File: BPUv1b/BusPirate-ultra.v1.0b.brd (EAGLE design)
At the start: 100 x 50 mm, 171 parts, among them IC1 23LC1024, IC10 SN74LVC1T45DBV, IC11 SN74LVC1T45DBV, IC12 74LVC1G07DBV, IC13 SN74LVC1T45DBV, IC17 74LVC1G07DBV, IC18 SN74LVC1T45DBV, IC19 74LVC1G07DBV, IC2 23LC1024, IC20 SN74LVC1T45DBV, IC21 74LVC1G07DBV, IC22 SN74LVC1T45DBV, IC23 MCP1824_ADJ, IC24 74HCT4051, IC4 74LVC1G07DBV, IC5 74LVC1G07DBV, IC6 74LVC1G07DBV, IC7 74LVC1G07DBV, IC8 SN74LVC1T45DBV, IC9 SN74LVC1T45DBV, J1 CON_MOLEX_MALE_SMT_SH_1.25, J2 CON_HEADER_1X04, J4 CON_HEADER_1X10-RIGHT_ANGLED_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, Q1 DMMT3906W, U1 W25X40CL, U2 STM32F103ZX, U3 ICE40HX4K, U4 MCP6001, U5 74LVC245A, U7 MCP6001, U8 74HCT4066PW, U9 74HCT4066PW

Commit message: continue routing
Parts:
- removed R10, R7, R8, R9: 10K, resistor:R0603
- added RN1: 10K, dp_devices:RN8P-4R-CRA06S
- moved R44 4.83 mm to (34.7, 3.94)
- moved R41 4.70 mm to (69.1, 7.75), turned to 0 degrees
- moved Q1 4.04 mm to (37.5, 3.81), turned to 90 degrees
- moved R43 4.03 mm to (40.3, 3.81), turned to 90 degrees
- moved C60 3.94 mm to (72.1, 7.75), turned to 0 degrees
- moved Q2 3.90 mm to (37.3, 7.49)
- moved C59 3.86 mm to (67.1, 6.60), turned to 270 degrees
- moved R38 3.49 mm to (79.0, 8.89), turned to 0 degrees
- moved C9 2.79 mm to (29.8, 11.7)
- moved C58 2.47 mm to (82.3, 7.75), turned to 0 degrees
- moved C55 2.42 mm to (68.3, 16.5)
- moved R35 2.42 mm to (71.4, 16.5), turned to 0 degrees
- moved C3 2.29 mm to (33.8, 11.6)
- moved C56 2.07 mm to (74.4, 16.5), turned to 0 degrees
- moved IC21 2.03 mm to (70.4, 3.05)
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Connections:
- removed net N$65: R51.2, R9.1
- new net N$21: R51.2, RN1.4
- net ADC1: now also RN1.5, RN1.6; no longer R10.2, R9.2
- net GND: now also RN1.2, RN1.3; no longer R10.1, R8.1
- net MCU_ADC6: now also RN1.7, RN1.8; no longer R7.2, R8.2
- net VREF/VOUT: now also RN1.1; no longer R7.1
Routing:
- net VUSB: track 120.9 -> 258.8 mm, vias 7 -> 14
- net VREF/VOUT: track 56.3 -> 117.6 mm, vias 0 -> 2
- net N$26: track 0.00 -> 23.7 mm, vias 0 -> 4
- net ADC1: track 32.3 -> 10.6 mm, vias 2 -> 0
- net MCU_ADC6: track 0.00 -> 21.3 mm, vias 0 -> 2
- net MCU_VPU: track 0.00 -> 15.2 mm, vias 0 -> 4
- net N$11: track 0.00 -> 6.62 mm
- net N$21: track 0.00 -> 6.62 mm
- net N$12: track 0.00 -> 5.77 mm
- net N$25: track 0.00 -> 3.90 mm
- net N$27: track 0.00 -> 3.49 mm
- net BUFOD7: track 25.1 -> 21.7 mm
- net 3V3: track 409.2 -> 406.7 mm, vias 33 -> 35
- net BUFDIR7: track 24.5 -> 22.4 mm
- net BUFIO7: track 20.8 -> 18.8 mm
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- added copper zone on layer 1, net N$26
- added copper zone on layer 1, net VREF/VOUT

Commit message: routed power traces
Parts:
- moved C48 2.34 mm to (82.5, 16.5), turned to 180 degrees
- moved C54 1.35 mm to (71.1, 26.9)
- moved R32 1.30 mm to (82.5, 17.7)
- moved R42 1.14 mm to (75.1, 3.81), turned to 90 degrees
- moved R39 0.89 mm to (85.2, 3.30)
- moved C42 0.65 mm to (79.2, 16.5), turned to 0 degrees
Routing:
- net 3V3: track 406.7 -> 562.3 mm, vias 35 -> 64
- net VREF/VOUT: track 117.6 -> 186.4 mm, vias 2 -> 14
- net MCU_VPU: track 15.2 -> 53.0 mm, vias 4 -> 6
- net BPIO7: track 52.5 -> 59.0 mm
- net BPIO1: track 62.1 -> 59.1 mm, vias 3 -> 4
- net BPIO4: track 54.7 -> 57.7 mm
- net N$5: track 8.93 -> 11.2 mm
- net BPIO6: track 56.0 -> 58.2 mm, vias 4 -> 5
- net VUSB: track 258.8 -> 256.9 mm
- net BUFDIR4: track 21.1 -> 22.3 mm
- net BUFDIR7: track 22.4 -> 21.3 mm
- net BUFIO4: track 17.5 -> 18.3 mm
- net BUFDIR1: track 19.1 -> 19.7 mm
- net BUFOD4: track 19.3 -> 19.8 mm

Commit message: continue routing
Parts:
- R6: device dp_devices:R603 -> rcl:R0603
- moved R16 11.5 mm to (51.3, 7.87), turned to 180 degrees
- moved R15 9.45 mm to (50.8, 10.4)
- moved R51 4.45 mm to (44.2, 3.43)
- moved C22 2.95 mm to (63.0, 11.2), flipped to the bottom
- moved C14 2.85 mm to (47.6, 4.95), turned to 270 degrees
- moved R6 2.01 mm to (65.9, 12.1), turned to 90 degrees
- moved C30 1.37 mm to (48.8, 10.4)
- moved C51 1.14 mm to (49.7, 4.95), turned to 270 degrees
- moved C33 0.80 mm to (46.7, 10.4)
- moved RN1 0.76 mm to (44.2, 6.60)
- moved Q2 0.51 mm to (37.3, 6.99)
- moved Q1 0.25 mm to (37.5, 3.56)
- moved R43 0.25 mm to (40.3, 3.56)
- moved R44 0.25 mm to (34.7, 3.68)
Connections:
- net FPGA_PROG_CS: now also R6.2; no longer R6.1
- net GND: now also R6.1; no longer R6.2
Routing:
- net MCU_VPU: track 53.0 -> 119.5 mm, vias 6 -> 9
- net N$61: track 0.00 -> 42.5 mm, vias 0 -> 4
- net ADC1: track 10.6 -> 31.4 mm, vias 0 -> 2
- net MCU_ADC6: track 21.3 -> 34.8 mm
- net 3V3: track 562.3 -> 557.5 mm
- net N$21: track 6.62 -> 2.01 mm
- net N$64: track 5.97 -> 10.5 mm
- net FPGA_PROG_CS: track 36.4 -> 38.9 mm
- net BPIO6: track 58.2 -> 60.7 mm, vias 5 -> 3
- net FPGA_CRESET: track 33.0 -> 35.3 mm, vias 2 -> 3
- net N$26: track 23.7 -> 25.5 mm
- net BUFIO7: track 18.8 -> 17.2 mm
- net BUFDIR7: track 21.3 -> 19.9 mm
- net BUFIO6: track 28.4 -> 27.0 mm
- net BUFOD6: track 31.5 -> 30.2 mm
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
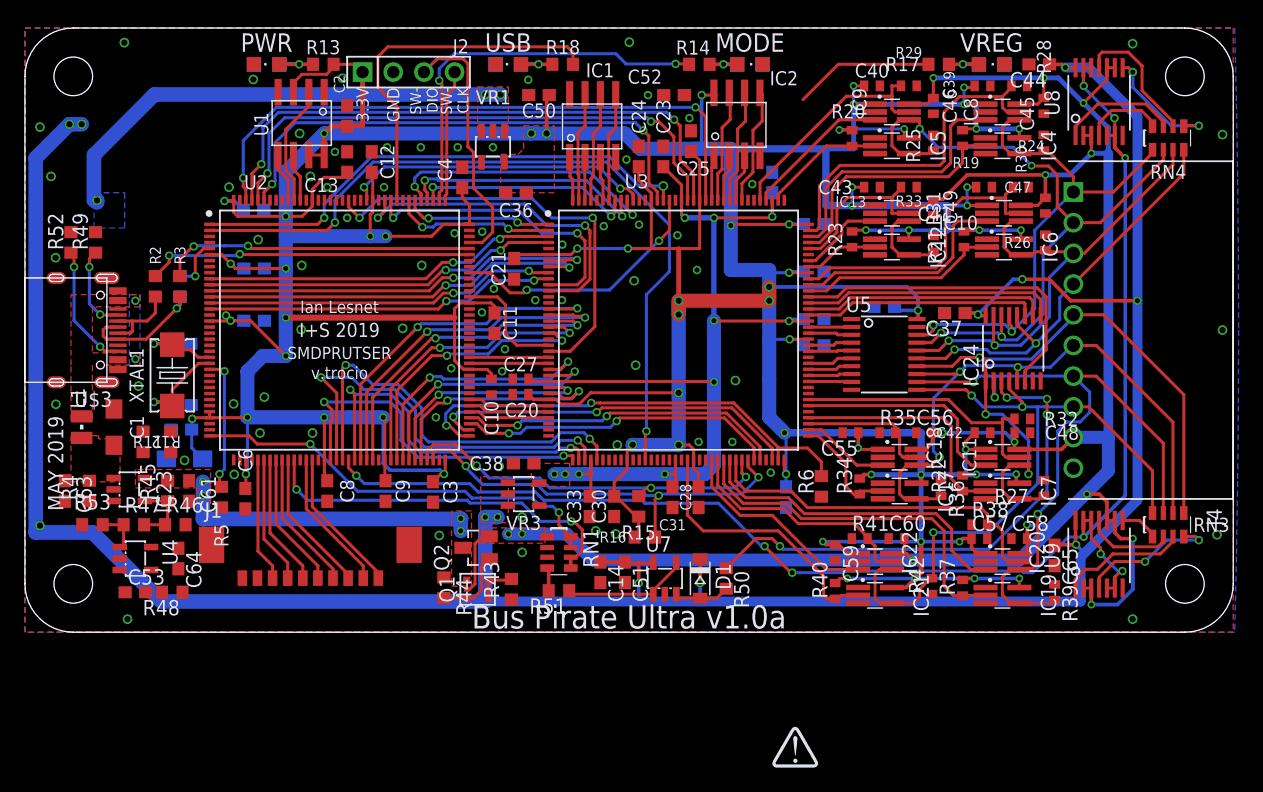
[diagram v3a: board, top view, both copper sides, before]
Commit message: board routing done, add usbc bottom PTH chassis mount library
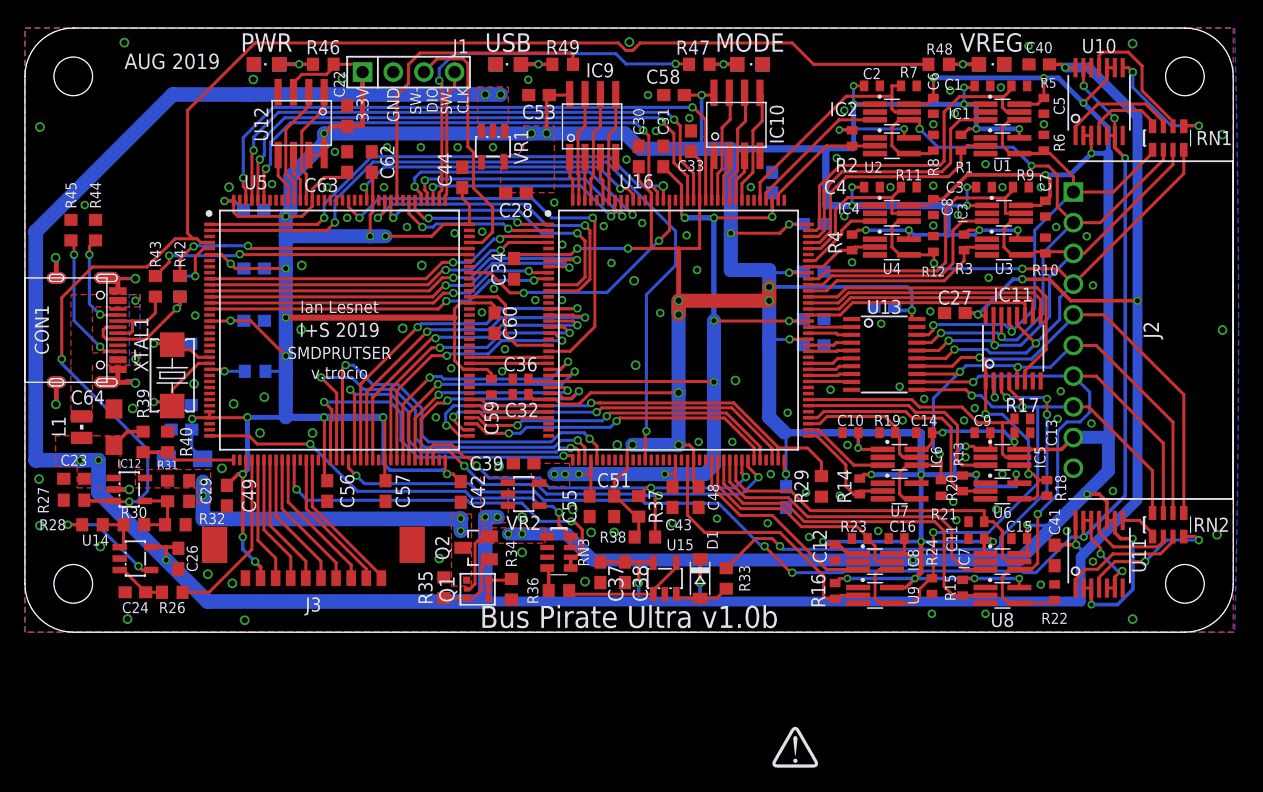
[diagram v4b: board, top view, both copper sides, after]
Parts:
- removed C65: 0.1uF, rcl:C0603
- removed IC13, IC18, IC20, IC22: SN74LVC1T45DBV, dp_devices.v6:SC-70-6_EXTENDED_PADS
- removed IC17, IC19, IC21: 74LVC1G07DBV, dp_devices.v6:SC-70-5_EXTENDED_PADS
- removed IC23: MCP1824_ADJ, dp_devices.v6:SOT-23-5
- removed IC24: 74HCT4051, dp_devices.v6:TSSOP-16
- removed J4: CON_HEADER_1X10-RIGHT_ANGLED_PTH_SHROUDED, dp_devices.v6:M1X10_MALE_RIGHT_ANGLES_PTH_SHROUDED
- removed R50, R51: (no value), resistor:R0603
- removed R52: 5K1, rcl:R0603
- removed R53: 0R, dp_devices.v6:R603
- removed RN4: 2K, dp_devices:RN8P-4R-CRA06S
- added C62: 0.1uF, rcl:C0603
- added IC3: SN74LVC1T45DBV, dp_devices.v6:SC-70-6_EXTENDED_PADS
- added J3: CON_MOLEX_MALE_SMT_SH_1.25, dp_devices.v6:MOLEX_533980771
- added R10, R8: 1M, resistor:R0402
- added R7, R9: 100K, resistor:R0402
- added RN2: 2K, dp_devices:RN8P-4R-CRA06S
- added U10, U11: 74HCT4066PW, dp_devices.v6:TSSOP-14
- added U12: W25X40CL, dp_devices.v6:SOIC-8
- added U13: 74LVC245A, dp_devices.v6:TSSOP-20
- added U14, U15: MCP6001, dp_devices.v6:SOT-23-5
- added U16: ICE40HX4K, dp_devices.v6:TQFP-144
- added U6: 74LVC1G07DBV, dp_devices.v6:SC-70-5_EXTENDED_PADS
- C1: value 10uF -> 0.1uF; device rcl:SMC_A -> rcl:C0402
- C10: device dp_devices.v6:C402 -> resistor:C0402
- C11, C12, C13, C14, C15, C2, C3, C4, C6, C7, C8, C9: device rcl:C0603 -> resistor:C0402
- C16: value 22pF -> 0.1uF; device rcl:C0603 -> resistor:C0402
- C17: value 1uF -> 0.1uF; device rcl:SMC_A -> rcl:C0603
- C19: value 0.1uF -> 1uF; device rcl:C0603 -> rcl:SMC_A
- C20: value 0.1uF -> 22pF; device dp_devices.v6:C402 -> rcl:C0603
- C23: value 0.1uF -> 10uF; device rcl:C0603 -> dp_devices.v6:C603
- C24: value 0.1uF -> (none)
- C27: device dp_devices.v6:C402 -> rcl:C0603
- C28: value 0.1uF -> 1uf
- C29: value 0.1uF -> 1uF; device rcl:C0603 -> dp_devices.v6:C603
- C32: device rcl:C0603 -> dp_devices.v6:C402
- C36: value 1uf -> 0.1uF; device rcl:C0603 -> dp_devices.v6:C402
- C38: value 1uf -> 1uF
- C39: value 0.1uF -> 1uf; device rcl:C0402 -> rcl:C0603
- C40, C41, C42, C43, C46, C47, C48, C49, C55, C56, C57, C58, C60: device resistor:C0402 -> rcl:C0603
- C45: device rcl:C0402 -> rcl:C0603
- C5: device rcl:C0603 -> rcl:C0402
- C51: value 1uF -> 0.1uF
- C53: value (none) -> 0.1uF
- C59: device resistor:C0402 -> dp_devices.v6:C402
- C61: value 1uF -> 0.1uF; device dp_devices.v6:C603 -> rcl:C0603
- C63: value 10uF -> 0.1uF; device dp_devices.v6:C603 -> rcl:C0603
- C64: value 0.1uF -> 10uF; device rcl:C0603 -> rcl:SMC_A
- IC1, IC2: value 23LC1024 -> SN74LVC1T45DBV; device dp_devices:SOIC-8 -> dp_devices.v6:SC-70-6_EXTENDED_PADS
- IC10, IC9: value SN74LVC1T45DBV -> 23LC1024; device dp_devices.v6:SC-70-6_EXTENDED_PADS -> dp_devices:SOIC-8
- IC11: value SN74LVC1T45DBV -> 74HCT4051; device dp_devices.v6:SC-70-6_EXTENDED_PADS -> dp_devices.v6:TSSOP-16
- IC12: value 74LVC1G07DBV -> MCP1824_ADJ; device dp_devices.v6:SC-70-5_EXTENDED_PADS -> dp_devices.v6:SOT-23-5
- IC4, IC5, IC6, IC7: value 74LVC1G07DBV -> SN74LVC1T45DBV; device dp_devices.v6:SC-70-5_EXTENDED_PADS -> dp_devices.v6:SC-70-6_EXTENDED_PADS
- J1: value CON_MOLEX_MALE_SMT_SH_1.25 -> CON_HEADER_1X04; device dp_devices.v6:MOLEX_533980771 -> dp_devices.v6:M1X4
- J2: value CON_HEADER_1X04 -> CON_HEADER_1X10-RIGHT_ANGLED_PTH_SHROUDED; device dp_devices.v6:M1X4 -> dp_devices.v6:M1X10_MALE_RIGHT_ANGLES_PTH_SHROUDED
- R1: value 1.5K -> 100K; device rcl:R0603 -> resistor:R0402
- R11: value 10K -> 100K; device resistor:R0603 -> resistor:R0402
- R12: value 10K -> 1M; device resistor:R0603 -> resistor:R0402
- R13, R14, R17: value 1K1 -> 100K; device dp_devices:R603 -> resistor:R0402
- R15, R16: value 10K -> 100K; device rcl:R0603 -> resistor:R0402
- R18: value 1K1 -> 1M; device dp_devices:R603 -> resistor:R0402
- R2, R3: value 22R -> 100K; device rcl:R0603 -> resistor:R0402
- R20, R22: value 100K -> 1M
- R25, R27: value 1M -> 10K; device resistor:R0402 -> dp_devices.v6:R603
- R26: value 1M -> (none); device resistor:R0402 -> rcl:R0603
- R28: value 100K -> 0R; device resistor:R0402 -> dp_devices.v6:R603
- R29, R37, R38: value 100K -> 10K; device resistor:R0402 -> rcl:R0603
- R30: value 100K -> 78.7K; device resistor:R0402 -> dp_devices.v6:R603
- R31: value 1M -> 100K; device resistor:R0402 -> dp_devices.v6:R603
- R32: value 100K -> 50K; device resistor:R0402 -> dp_devices.v6:R603
- R33: value 100K -> (none); device resistor:R0402 -> resistor:R0603
- R34, R35: value 100K -> (none); device resistor:R0402 -> dp_devices.v6:R603
- R36: value 1M -> (none); device resistor:R0402 -> resistor:R0603
- R39: value 1M -> 10K; device resistor:R0402 -> resistor:R0603
- R4, R5: value 10K -> 100K; device dp_devices.v6:R603 -> resistor:R0402
- R40: value 100K -> 10K; device resistor:R0402 -> resistor:R0603
- R41: value 100K -> 1.5K; device resistor:R0402 -> rcl:R0603
- R42: value 1M -> 22R; device resistor:R0402 -> rcl:R0603
- R43: value (none) -> 22R; device dp_devices.v6:R603 -> rcl:R0603
- R44: value (none) -> 5K1; device dp_devices.v6:R603 -> rcl:R0603
- R45: value 100K -> 5K1; device dp_devices.v6:R603 -> rcl:R0603
- R46: value 50K -> 1K1; device dp_devices.v6:R603 -> dp_devices:R603
- R47: value 78.7K -> 1K1; device dp_devices.v6:R603 -> dp_devices:R603
- R48: value (none) -> 1K1; device rcl:R0603 -> dp_devices:R603
- R49: value 5K1 -> 1K1; device rcl:R0603 -> dp_devices:R603
- R6: value 10K -> 1M; device rcl:R0603 -> resistor:R0402
- RN1: value 10K -> 2K
- RN3: value 2K -> 10K
- U1: value W25X40CL -> 74LVC1G07DBV; device dp_devices.v6:SOIC-8 -> dp_devices.v6:SC-70-5_EXTENDED_PADS
- U2: value STM32F103ZX -> 74LVC1G07DBV; device dp_devices.v6:TQFP-144 -> dp_devices.v6:SC-70-5_EXTENDED_PADS
- U3: value ICE40HX4K -> 74LVC1G07DBV; device dp_devices.v6:TQFP-144 -> dp_devices.v6:SC-70-5_EXTENDED_PADS
- U4, U7: value MCP6001 -> 74LVC1G07DBV; device dp_devices.v6:SOT-23-5 -> dp_devices.v6:SC-70-5_EXTENDED_PADS
- U5: value 74LVC245A -> STM32F103ZX; device dp_devices.v6:TSSOP-20 -> dp_devices.v6:TQFP-144
- U8, U9: value 74HCT4066PW -> 74LVC1G07DBV; device dp_devices.v6:TSSOP-14 -> dp_devices.v6:SC-70-5_EXTENDED_PADS
- moved R28 84.9 mm to (5.59, 8.89), turned to 0 degrees
- moved R27 80.3 mm to (4.06, 10.9), turned to 180 degrees
- moved R30 78.5 mm to (9.02, 8.89), turned to 0 degrees
- moved R26 77.8 mm to (12.2, 3.30), turned to 180 degrees
- moved C1 77.2 mm to (79.2, 45.2), turned to 0 degrees
- moved R48 77.0 mm to (75.6, 47.0)
- moved R39 76.5 mm to (9.78, 15.7)
- moved R5 74.3 mm to (82.3, 45.2), turned to 180 degrees
- moved R32 70.6 mm to (12.4, 8.89), turned to 0 degrees
- moved C15 69.9 mm to (82.3, 7.75), flipped to the top, turned to 0 degrees
- moved J2 68.7 mm to (93.2, 25.0), turned to 270 degrees
- moved U4 67.7 mm to (71.8, 31.9)
- moved R12 67.4 mm to (75.2, 32.1)
- moved R42 67.0 mm to (12.8, 28.6), turned to 270 degrees
- moved R31 66.6 mm to (11.8, 11.7), turned to 90 degrees
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- renumbered U$3 to CON1, VR3 to VR2
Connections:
- net 1V2: now also C36.1, C39.1, C43.2, C54.2, C55.2, U16.111, U16.126, U16.27, U16.40, U16.54, U16.92; no longer C23.2, C26.2, C27.1, C33.2, C38.1, U3.111, U3.126, U3.27, U3.40, U3.54, U3.92
- net 3V3: now also C1.1, C11.1, C12.1, C17.2, C19.+, C2.1, C28.1, C3.1, C32.1, C33.2, C4.1, C42.2, C44.2, C45.2, C46.2, C47.2, C48.2, C49.2, C50.2, C51.2, C52.2, C53.1, C56.2, C57.2, C58.1, C60.2, C61.1, C62.2, C63.2, C9.1, IC1.1, IC10.8, IC2.1, IC3.1, IC4.1, IC5.1, IC6.1, IC7.1, IC9.8, J1.1, J3.P9, R1.2, R14.2, R2.2, R25.2, R3.2, R38.2, R4.2, R46.2, U1.5, U12.3, U12.7, U12.8, U13.20, U16.100, U16.108, U16.123, U16.131, U16.30, U16.46, U16.57, U16.6, U16.72, U16.89, U2.5, U3.5, U4.5, U5.108, U5.121, U5.131, U5.144, U5.17, U5.32, U5.33, U5.39, U5.52, U5.6, U5.62, U5.72, U5.84, U5.95, U6.5, U7.5, U8.5, U9.5; no longer C11.2, C12.2, C13.2, C15.2, C17.+, C19.2, C2.2, C20.1, C24.2, C28.2, C29.2, C3.2, C32.2, C36.1, C39.1, C4.2, C40.1, C41.1, C42.1, C43.1, C5.2, C50.1, C52.1, C54.1, C55.1, C57.1, C6.2, C7.2, C8.2, C9.2, IC1.8, IC10.1, IC11.1, IC12.5, IC13.1, IC17.5, IC18.1, IC19.5, IC2.8, IC20.1, IC21.5, IC22.1, IC4.5, IC5.5, IC6.5, IC7.5, IC9.1, J1.P9, J2.1, R19.2, R20.2, R21.2, R22.2, R23.2, R34.2, R40.2, R5.2, U1.3, U1.7, U1.8, U2.108, U2.121, U2.131, U2.144, U2.17, U2.32, U2.33, U2.39, U2.52, U2.6, U2.62, U2.72, U2.84, U2.95, U3.100, U3.108, U3.123, U3.131, U3.30, U3.46, U3.57, U3.6, U3.72, U3.89, U5.20
- net ADC1: now also RN3.5, RN3.6, U5.47; no longer RN1.5, RN1.6, U2.47
- net ADC_MUX_EN: now also IC11.6, U16.96; no longer IC24.6, U3.96
- net ADC_MUX_S0: now also IC11.11, U16.93; no longer IC24.11, U3.93
- net ADC_MUX_S1: now also IC11.10, U16.94; no longer IC24.10, U3.94
- net ADC_MUX_S2: now also IC11.9, U16.95; no longer IC24.9, U3.95
- net BPIO0: now also IC1.4, IC11.13, J2.1, R6.2, RN1.1, U1.4, U13.18; no longer IC24.13, IC4.4, IC8.4, J4.1, R24.2, RN4.1, U5.18
- net BPIO1: now also IC11.14, IC2.4, J2.2, R8.2, RN1.2, U13.17, U2.4; no longer IC24.14, IC5.4, IC9.4, J4.2, R25.2, RN4.2, U5.17
- net BPIO2: now also IC11.15, IC3.4, J2.3, R10.2, RN1.3, U13.16, U3.4; no longer IC10.4, IC24.15, IC6.4, J4.3, R26.2, RN4.3, U5.16
- net BPIO3: now also IC11.12, IC4.4, J2.4, R12.2, RN1.4, U13.15, U4.4; no longer IC12.4, IC13.4, IC24.12, J4.4, R31.2, RN4.4, U5.15
- net BPIO4: now also IC11.1, IC5.4, J2.5, R18.2, RN2.5, U13.14, U6.4; no longer IC11.4, IC24.1, IC7.4, J4.5, R27.2, RN3.5, U5.14
- net BPIO5: now also IC11.5, IC6.4, J2.6, R20.2, RN2.6, U13.13, U7.4; no longer IC17.4, IC18.4, IC24.5, J4.6, R36.2, RN3.6, U5.13
- net BPIO6: now also IC11.2, IC7.4, J2.7, R22.2, RN2.7, U13.12, U8.4; no longer IC19.4, IC20.4, IC24.2, J4.7, R39.2, RN3.7, U5.12
- net BPIO7: now also IC11.4, IC8.4, J2.8, R24.2, RN2.8, U13.11, U9.4; no longer IC21.4, IC22.4, IC24.4, J4.8, R42.2, RN3.8, U5.11
- net BUFDIR0: now also IC1.5, R5.2, U16.107; no longer IC8.5, R28.2, U3.107
- net BUFDIR1: now also IC2.5, R7.2, U16.113; no longer IC9.5, R29.2, U3.113
- net BUFDIR2: now also IC3.5, R9.2, U16.99; no longer IC10.5, R30.2, U3.99
- net BUFDIR3: now also IC4.5, R11.2, U16.104; no longer IC13.5, R33.2, U3.104
- net BUFDIR4: now also IC5.5, R17.2, U16.79; no longer IC11.5, R32.2, U3.79
- net BUFDIR5: now also IC6.5, R19.2, U16.75; no longer IC18.5, R35.2, U3.75
- net BUFDIR6: now also IC7.5, R21.2, U16.64; no longer IC20.5, R38.2, U3.64
- net BUFDIR7: now also IC8.5, R23.2, U16.61; no longer IC22.5, R41.2, U3.61
- net BUFIO0: now also IC1.3, U16.106; no longer IC8.3, U3.106
- net BUFIO1: now also IC2.3, U16.112; no longer IC9.3, U3.112
- net BUFIO2: now also IC3.3, U16.98; no longer IC10.3, U3.98
- net BUFIO3: now also IC4.3, U16.102; no longer IC13.3, U3.102
- net BUFIO4: now also IC5.3, U16.78; no longer IC11.3, U3.78
- net BUFIO5: now also IC6.3, U16.74; no longer IC18.3, U3.74
- net BUFIO6: now also IC7.3, U16.63; no longer IC20.3, U3.63
- net BUFIO7: now also IC8.3, U16.60; no longer IC22.3, U3.60
- net BUFOD0: now also R1.1, U1.2, U16.105; no longer IC4.2, R19.1, U3.105
- net BUFOD1: now also R2.1, U16.110, U2.2; no longer IC5.2, R20.1, U3.110
- net BUFOD2: now also R3.1, U16.97, U3.2; no longer IC6.2, R21.1, U3.97
- net BUFOD3: now also R4.1, U16.101, U4.2; no longer IC12.2, R23.1, U3.101
- net BUFOD4: now also R13.1, U16.76, U6.2; no longer IC7.2, R22.1, U3.76
- net BUFOD5: now also R14.1, U16.73, U7.2; no longer IC17.2, R34.1, U3.73
- net BUFOD6: now also R15.1, U16.62, U8.2; no longer IC19.2, R37.1, U3.62
- net BUFOD7: now also R16.1, U16.56, U9.2; no longer IC21.2, R40.1, U3.56
- net D+: now also R41.1, R42.2; no longer R1.1, R3.2
- net D-: now also R43.2; no longer R2.2
- net DISPLAY_AUX1: now also J3.P5, U5.44; no longer J1.P5, U2.44
- net DISPLAY_AUX2: now also J3.P4, U5.45; no longer J1.P4, U2.45
- net DISPLAY_CS: now also J3.P1, U5.50; no longer J1.P1, U2.50
- net DISPLAY_D/P: now also J3.P2, U5.49; no longer J1.P2, U2.49
- net DISPLAY_PWM: now also J3.P3, U5.46; no longer J1.P3, U2.46
- net DISPLAY_SPI_CLOCK: now also J3.P8, U5.41; no longer J1.P8, U2.41
- net DISPLAY_SPI_MISO: now also J3.P7, U5.42; no longer J1.P7, U2.42
- net DISPLAY_SPI_MOSI: now also J3.P6, U5.43; no longer J1.P6, U2.43
- net FLASH_CS: now also U12.1, U5.132; no longer U1.1, U2.132
- net FLASH_MISO: now also U12.2, U5.134; no longer U1.2, U2.134
- net FLASH_MOSI: now also U12.5, U5.135; no longer U1.5, U2.135
- net FLASH_SCK: now also U12.6, U5.133; no longer U1.6, U2.133
- net FPGA_CDONE: now also R37.1, U16.65, U5.69; no longer R15.1, U2.69, U3.65
- net FPGA_CRESET: now also R38.1, U16.66, U5.70; no longer R16.1, U2.70, U3.66
- net FPGA_PROG_CLOCK: now also U16.70, U5.74; no longer U2.74, U3.70
- net FPGA_PROG_CS: now also R29.2, U16.71, U5.73; no longer R6.2, U2.73, U3.71
- net FPGA_PROG_MISO: now also U16.67, U5.75; no longer U2.75, U3.67
- net FPGA_PROG_MOSI: now also U16.68, U5.76; no longer U2.76, U3.68
- net FSMC_A0: now also U16.3, U5.10; no longer U2.10, U3.3
- net FSMC_A1: now also U16.4, U5.11; no longer U2.11, U3.4
- net FSMC_A2: now also U16.7, U5.12; no longer U2.12, U3.7
- net FSMC_A3: now also U16.8, U5.13; no longer U2.13, U3.8
- net FSMC_A4: now also U16.9, U5.14; no longer U2.14, U3.9
- net FSMC_A5: now also U16.10, U5.15; no longer U2.15, U3.10
- net FSMC_D0: now also U16.24, U5.85; no longer U2.85, U3.24
- net FSMC_D1: now also U16.23, U5.86; no longer U2.86, U3.23
- net FSMC_D10: now also U16.26, U5.66; no longer U2.66, U3.26
- net FSMC_D11: now also U16.28, U5.67; no longer U2.67, U3.28
- net FSMC_D12: now also U16.29, U5.68; no longer U2.68, U3.29
- net FSMC_D13: now also U16.33, U5.77; no longer U2.77, U3.33
- net FSMC_D14: now also U16.32, U5.78; no longer U2.78, U3.32
- net FSMC_D15: now also U16.31, U5.79; no longer U2.79, U3.31
- net FSMC_D2: now also U16.1, U5.114; no longer U2.114, U3.1
- net FSMC_D3: now also U16.2, U5.115; no longer U2.115, U3.2
- net FSMC_D4: now also U16.15, U5.58; no longer U2.58, U3.15
- net FSMC_D5: now also U16.16, U5.59; no longer U2.59, U3.16
- net FSMC_D6: now also U16.17, U5.60; no longer U2.60, U3.17
- net FSMC_D7: now also U16.18, U5.63; no longer U2.63, U3.18
- net FSMC_D8: now also U16.19, U5.64; no longer U2.64, U3.19
- net FSMC_D9: now also U16.25, U5.65; no longer U2.65, U3.25
- net FSMC_NE3_CE: now also U16.22, U5.125; no longer U2.125, U3.22
- net FSMC_NOE_OE: now also U16.11, U5.118; no longer U2.118, U3.11
- net FSMC_NWE_WE: now also U16.12, U5.119; no longer U2.119, U3.12
- net GND: now also C1.2, C11.2, C12.2, C14.1, C17.1, C19.-, C2.2, C20.1, C23.2, C24.2, C26.2, C28.2, C29.2, C3.2, C32.2, C4.2, C42.1, C43.1, C44.1, C50.1, C51.1, C52.1, C54.1, C55.1, C57.1, C58.2, C62.1, C63.1, C64.-, C9.2, CON1.P$5, CON1.P$6, CON1.P$7, CON1.P$8, IC1.2, IC10.4, IC11.7, IC11.8, IC12.2, IC2.2, IC3.2, IC4.2, IC5.2, IC6.2, IC7.2, IC9.4, J1.2, J2.10, J3.P10, R10.1, R11.1, R17.1, R18.1, R19.1, R20.1, R21.1, R22.1, R23.1, R27.2, R32.2, R34.1, R40.1, R44.2, R45.2, R5.1, R7.1, R8.1, R9.1, RN3.2, RN3.3, U1.3, U10.7, U11.7, U12.4, U13.1, U13.10, U13.19, U14.2, U15.2, U16.103, U16.127, U16.13, U16.132, U16.14, U16.140, U16.5, U16.53, U16.59, U16.69, U16.86, U2.3, U3.3, U4.3, U5.107, U5.120, U5.130, U5.138, U5.143, U5.16, U5.30, U5.31, U5.38, U5.48, U5.51, U5.61, U5.71, U5.83, U5.94, U6.3, U7.3, U8.3, U9.3; no longer C1.-, C11.1, C12.1, C14.2, C17.-, C19.1, C2.1, C20.2, C23.1, C24.1, C26.1, C28.1, C29.1, C3.1, C32.1, C4.1, C42.2, C43.2, C44.2, C50.2, C51.2, C52.2, C54.2, C55.2, C57.2, C58.1, C63.2, C64.2, C65.2, C9.1, IC1.4, IC10.2, IC11.2, IC12.3, IC13.2, IC17.3, IC18.2, IC19.3, IC2.4, IC20.2, IC21.3, IC22.2, IC23.2, IC24.7, IC24.8, IC4.3, IC5.3, IC6.3, IC7.3, IC9.2, J1.P10, J2.2, J4.10, R25.1, R26.1, R27.1, R28.1, R30.1, R31.1, R32.1, R33.1, R36.1, R38.1, R39.1, R4.2, R41.1, R42.1, R43.1, R44.1, R46.2, R49.2, R52.2, RN1.2, RN1.3, U1.4, U2.107, U2.120, U2.130, U2.138, U2.143, U2.16, U2.30, U2.31, U2.38, U2.48, U2.51, U2.61, U2.71, U2.83, U2.94, U3.103, U3.127, U3.13, U3.132, U3.14, U3.140, U3.5, U3.53, U3.59, U3.69, U3.86, U4.2, U5.1, U5.10, U5.19, U7.2, U8.7, U9.7
- net LAT0: now also U13.2, U16.91; no longer U3.91, U5.2
- net LAT1: now also U13.3, U16.90; no longer U3.90, U5.3
- net LAT2: now also U13.4, U16.88; no longer U3.88, U5.4
- net LAT3: now also U13.5, U16.87; no longer U3.87, U5.5
- net LAT4: now also U13.6, U16.85; no longer U3.85, U5.6
- net LAT5: now also U13.7, U16.84; no longer U3.84, U5.7
- net LAT6: now also U13.8, U16.83; no longer U3.83, U5.8
- net LAT7: now also U13.9, U16.82; no longer U3.82, U5.9
- net LD1: now also R47.2, U5.110; no longer R14.2, U2.110
- net MCU_ADC5: now also R39.2, R40.2, U5.37; no longer R11.2, R12.2, U2.37
- net MCU_ADC6: now also RN3.7, RN3.8, U5.36; no longer RN1.7, RN1.8, U2.36
- net MCU_AUX1: now also U16.137, U5.111; no longer U2.111, U3.137
- net MCU_AUX10: now also U16.38, U5.57; no longer U2.57, U3.38
- net MCU_AUX11: now also U16.39, U5.54; no longer U2.54, U3.39
- net MCU_AUX12: now also U16.41, U5.55; no longer U2.55, U3.41
- net MCU_AUX2: now also U16.136, U5.112; no longer U2.112, U3.136
- net MCU_AUX3: now also U16.135, U5.113; no longer U2.113, U3.135
- net MCU_AUX4: now also U16.134, U5.122; no longer U2.122, U3.134
- net MCU_AUX5: now also U16.130, U5.139; no longer U2.139, U3.130
- net MCU_AUX6: now also U16.125, U5.140; no longer U2.140, U3.125
- net MCU_AUX7: now also U16.124, U5.141; no longer U2.141, U3.124
- net MCU_AUX8: now also U16.122, U5.142; no longer U2.142, U3.122
- net MCU_AUX9: now also U16.37, U5.53; no longer U2.53, U3.37
- net MCU_INT0: now also U16.129, U5.1; no longer U2.1, U3.129
- net MCU_INT1: now also U16.49, U5.2; no longer U2.2, U3.49
- net MCU_MCO: now also U16.128, U5.100; no longer U2.100, U3.128
- net MCU_VPU: now also U10.12, U10.13, U10.5, U10.6, U11.12, U11.13, U11.5, U11.6, U5.56; no longer U2.56, U8.12, U8.13, U8.5, U8.6, U9.12, U9.13, U9.5, U9.6
- net N$10: now also U5.35; no longer U2.35
- net N$11: now also R35.2; no longer R44.2
- net N$12: now also IC12.4, R30.2, R31.1, R32.1; no longer IC23.4, R45.1, R46.1, R47.2
- net N$13: now also R49.1; no longer R18.1
- net N$14: now also R44.1; no longer R49.1
- net N$15: now also R28.1, U14.4; no longer R53.1, U4.4
- net N$16: now also U5.9; no longer U2.9
- net N$17: now also U16.34; no longer U3.34
- net N$18: now also R48.1; no longer R17.1
- net N$19: now also U5.97; no longer U2.97
- net N$2: now also RN1.7, U10.1; no longer RN4.7, U8.1
- net N$20: now also R45.1; no longer R52.1
- net N$21: now also R36.2, RN3.4; no longer R51.2, RN1.4
- net N$22: now also U5.98; no longer U2.98
- net N$23: now also U5.28; no longer U2.28
- net N$25: now also R28.2, R30.1, U14.1; no longer R47.1, R53.2, U4.1
- net N$26: now also C29.1, IC12.5, R31.2; no longer C61.1, IC23.5, R45.2
- net N$27: now also R34.2; no longer R43.2
- net N$28: now also U5.80; no longer U2.80
- net N$29: now also U5.116; no longer U2.116
- net N$3: now also RN1.8, U10.4; no longer RN4.8, U8.4
- net N$30: now also U5.26; no longer U2.26
- net N$31: now also C24.1, R26.2, U14.3; no longer C53.1, R48.2, U4.3
- net N$32: now also R33.2, U15.3; no longer R50.2, U7.3
- net N$33: now also RN2.3, U11.1; no longer RN3.3, U9.1
- net N$34: now also U5.82; no longer U2.82
- net N$35: now also U5.27; no longer U2.27
- net N$36: now also U5.18; no longer U2.18
- net N$37: now also U5.19; no longer U2.19
- net N$38: now also U5.20; no longer U2.20
- net N$39: now also U5.21; no longer U2.21
- net N$4: now also RN1.5, U10.8; no longer RN4.5, U8.8
- net N$40: now also U5.22; no longer U2.22
- net N$41: now also U5.99; no longer U2.99
- net N$42: now also RN2.4, U11.4; no longer RN3.4, U9.4
- net N$43: now also U5.81; no longer U2.81
- net N$44: now also RN2.1, U11.8; no longer RN3.1, U9.8
- net N$45: now also RN2.2, U11.11; no longer RN3.2, U9.11
- net N$5: now also RN1.6, U10.11; no longer RN4.6, U8.11
- net N$52: now also U5.90; no longer U2.90
- net N$53: now also U5.93; no longer U2.93
- net N$54: now also U5.124; no longer U2.124
- net N$56: now also U5.123; no longer U2.123
- net N$57: now also U5.126; no longer U2.126
- net N$58: now also U5.127; no longer U2.127
- net N$59: now also U5.128; no longer U2.128
- net N$6: now also R47.1; no longer R14.1
- net N$60: now also U5.129; no longer U2.129
- net N$61: now also IC11.3, R33.1; no longer IC24.3, R50.1
- net N$64: now also R36.1, U15.1, U15.4; no longer R51.1, U7.1, U7.4
- net N$7: now also R46.1; no longer R13.1
- net N$8: now also C20.2, U5.23; no longer C18.2, U2.23
- net N$9: now also C18.2, U5.24; no longer C16.2, U2.24
- net PWM: now also U16.21, U5.96; no longer U2.96, U3.21
- net RST: now also R25.1, U5.25; no longer R5.1, U2.25
- net SRAM0_CLOCK: now also IC9.6, U16.141; no longer IC1.6, U3.141
- net SRAM0_CS: now also IC9.1, U16.144; no longer IC1.1, U3.144
- net SRAM0_SIO0: now also IC9.5, U16.138; no longer IC1.5, U3.138
- net SRAM0_SIO1: now also IC9.2, U16.142; no longer IC1.2, U3.142
- net SRAM0_SIO2: now also IC9.3, U16.139; no longer IC1.3, U3.139
- net SRAM0_SIO3: now also IC9.7, U16.143; no longer IC1.7, U3.143
- net SRAM1_CLOCK: now also IC10.6, U16.118; no longer IC2.6, U3.118
- net SRAM1_CS: now also IC10.1, U16.121; no longer IC2.1, U3.121
- net SRAM1_SIO0: now also IC10.5, U16.116; no longer IC2.5, U3.116
- net SRAM1_SIO1: now also IC10.2, U16.119; no longer IC2.2, U3.119
- net SRAM1_SIO2: now also IC10.3, U16.117; no longer IC2.3, U3.117
- net SRAM1_SIO3: now also IC10.7, U16.120; no longer IC2.7, U3.120
- net SWCLK: now also J1.4, U5.109; no longer J2.4, U2.109
- net SWDIO: now also J1.3, U5.105; no longer J2.3, U2.105
- net UART_RX: now also U5.102; no longer U2.102
- net UART_TX: now also U5.101; no longer U2.101
- net USBLED: now also R49.2, U5.117; no longer R18.2, U2.117
- net USB_D+: now also R42.1, U5.104; no longer R3.1, U2.104
- net USB_D-: now also R43.1, U5.103; no longer R2.1, U2.103
- net USB_DET: now also R41.2, U5.5; no longer R1.2, U2.5
- net VPP_FAST: now also U16.109; no longer U3.109
- net VREF/VOUT: now also C13.2, C14.2, C15.2, C16.2, C5.2, C6.2, C7.2, C8.2, IC1.6, IC2.6, IC3.6, IC4.6, IC5.6, IC6.6, IC7.6, J2.9, RN3.1, U10.10, U10.2, U10.3, U10.9, U11.10, U11.2, U11.3, U11.9; no longer C45.2, C46.2, C47.2, C48.2, C49.2, C56.2, C58.2, C60.2, IC10.6, IC11.6, IC13.6, IC18.6, IC20.6, IC22.6, IC9.6, J4.9, RN1.1, U8.10, U8.2, U8.3, U8.9, U9.10, U9.2, U9.3, U9.9
- net VREGEN: now also IC12.3, R27.1, R48.2, U5.4; no longer IC23.3, R17.2, R4.1, U2.4
- net VREG_DAC: now also R26.1, U5.40; no longer R48.1, U2.40
- net VUSB: now also C23.1, C26.1, C27.1, C38.1, C40.1, C41.1, C64.+, IC11.16, IC12.1, R39.1, U10.14, U11.14, U14.5, U15.5; no longer C1.+, C14.1, C44.1, C51.1, C63.1, C64.1, C65.1, IC23.1, IC24.16, R11.1, U4.5, U7.5, U8.14, U9.14
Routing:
- net VREGEN: track 11.6 -> 114.7 mm, vias 0 -> 2
- net GND: track 0.00 -> 22.1 mm, vias 72 -> 137
- net 3V3: track 557.5 -> 573.9 mm, vias 64 -> 65
- net VREG_DAC: track 0.00 -> 14.6 mm
- net BPIO3: track 41.7 -> 54.9 mm, vias 2 -> 4
- net FLASH_CS: track 0.00 -> 9.86 mm
- net N$15: track 0.00 -> 9.62 mm, vias 0 -> 2
- net RST: track 11.1 -> 2.98 mm, vias 2 -> 1
- net MCU_ADC5: track 0.02 -> 7.77 mm
- net N$31: track 0.00 -> 4.26 mm
- net USBLED: track 30.2 -> 26.5 mm
- net VUSB: track 257.7 -> 254.3 mm
- net BPIO4: track 57.4 -> 55.2 mm
- net N$14: track 7.19 -> 8.20 mm
- net N$20: track 10.4 -> 11.4 mm
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- removed copper zone on layer 16, net VUSB
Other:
- board text added: "AUG 2019"
- board text added: "Bus Pirate Ultra v1.0b"
- board text removed: "Bus Pirate Ultra v1.0a"
- board text removed: "MAY 2019"

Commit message: fix bom parts naming change back to original SC-70-5 and SC-70-6 footprints for 74LVC1G07DBV and SN74LVC1T45DBV added decoupling caps for open drain buffers(on going)
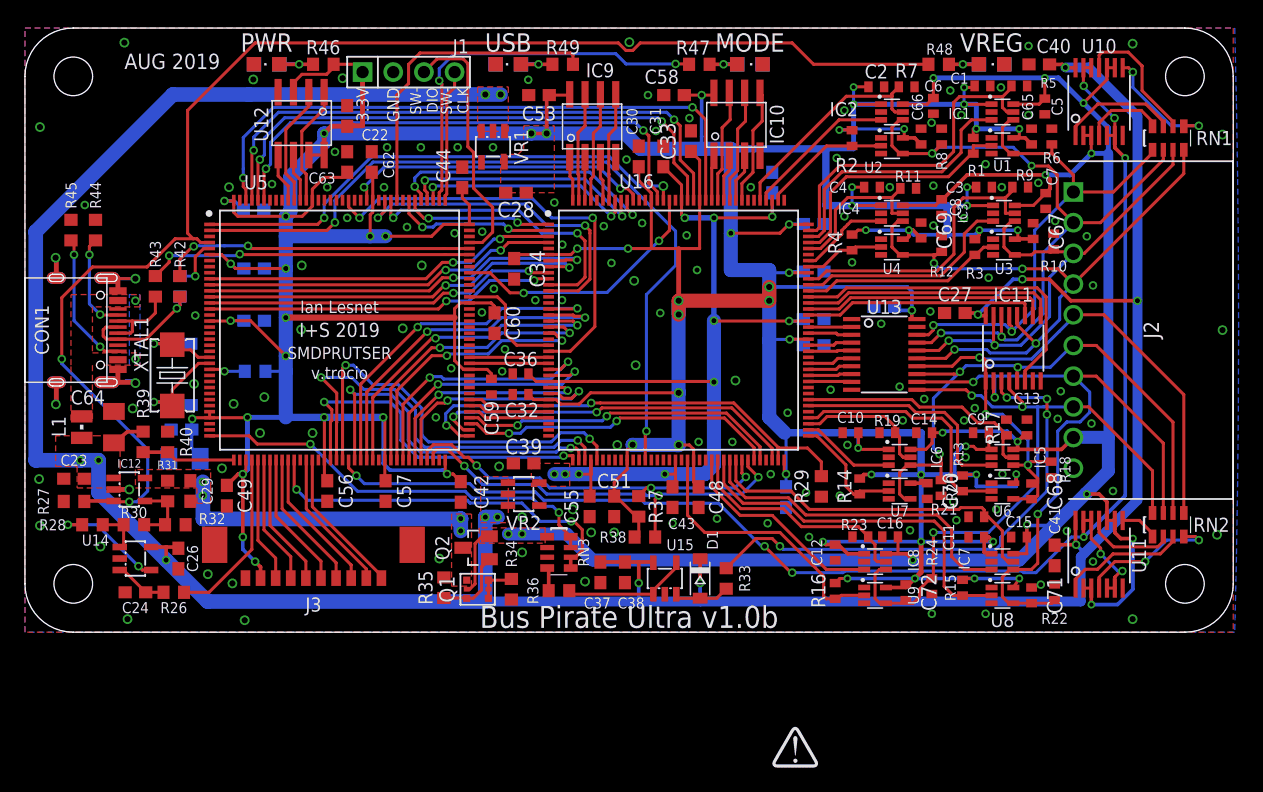
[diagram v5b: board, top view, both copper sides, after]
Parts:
- added C65, C66, C67, C68, C69, C70, C71, C72: 0.1uF, dp_devices.v6:C402
- C1, C5: device rcl:C0402 -> dp_devices.v6:C402
- C10, C11, C12, C13, C14, C15, C16, C2, C3, C4, C6, C7, C8, C9: device resistor:C0402 -> dp_devices.v6:C402
- C17, C18, C20, C21, C22, C24, C25, C26, C27, C30, C31, C33, C34, C35, C37, C38, C40, C41, C42, C43, C44, C45, C46, C47, C48, C49, C50, C51, C52, C53, C54, C55, C56, C57, C58, C60, C61, C62, C63: device rcl:C0603 -> dp_devices.v6:C603
- C19, C64: device rcl:SMC_A -> dp_devices.v6:SMC_A
- C28, C39: value 1uf -> 1uF; device rcl:C0603 -> dp_devices.v6:C603
- IC1, IC2, IC3, IC4, IC5, IC6, IC7, IC8: device dp_devices.v6:SC-70-6_EXTENDED_PADS -> dp_devices.v6:SC-70-6
- R1, R10, R11, R12, R13, R14, R15, R16, R17, R18, R19, R2, R20, R21, R22, R23, R24, R3, R4, R5, R6, R7, R8, R9: device resistor:R0402 -> dp_devices.v6:R402
- R26, R29, R37, R38, R41, R42, R43, R44, R45: device rcl:R0603 -> dp_devices.v6:R603
- R33, R36, R39, R40: device resistor:R0603 -> dp_devices.v6:R603
- R46, R47, R48, R49: device dp_devices:R603 -> dp_devices.v6:R603
- U1, U2, U3, U4, U6, U7, U8, U9: device dp_devices.v6:SC-70-5_EXTENDED_PADS -> dp_devices.v6:SC-70-5
- XTAL1: device dp_devices:XTAL_4X6 -> dp_devices.v6:XTAL_4X6
- moved R18 1.56 mm to (84.9, 13.5)
- moved R17 1.50 mm to (81.2, 16.9), turned to 270 degrees
- moved R1 1.05 mm to (78.5, 40.3)
- moved R3 0.97 mm to (78.6, 31.9)
- moved R8 0.85 mm to (75.9, 41.0)
- moved R6 0.83 mm to (85.0, 41.0)
- moved R10 0.76 mm to (85.1, 32.3)
- moved C8 0.69 mm to (75.9, 35.2), turned to 270 degrees
- moved R12 0.69 mm to (75.9, 32.1)
- moved C7 0.64 mm to (84.5, 35.7), turned to 270 degrees
- moved C13 0.58 mm to (82.9, 16.9), turned to 90 degrees
- moved C16 0.55 mm to (71.6, 7.90), turned to 180 degrees
- moved C36 0.43 mm to (41.0, 21.4)
- moved R21 0.41 mm to (78.7, 9.55)
- moved C2 0.36 mm to (70.5, 45.1), turned to 180 degrees
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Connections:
- net 1V2: now also C31.1, C35.1, C39.2, C43.1, C54.1, C55.1; no longer C31.2, C35.2, C39.1, C43.2, C54.2, C55.2
- net 3V3: now also C1.2, C10.2, C11.2, C12.2, C17.1, C2.2, C21.1, C22.1, C25.1, C28.2, C3.2, C30.1, C33.1, C34.1, C4.2, C42.1, C44.1, C45.1, C46.1, C47.1, C48.1, C49.1, C50.1, C51.1, C52.1, C53.2, C56.1, C57.1, C58.2, C60.1, C61.2, C62.1, C63.1, C65.2, C66.2, C67.2, C68.2, C69.2, C70.2, C71.2, C72.2, C9.2; no longer C1.1, C10.1, C11.1, C12.1, C17.2, C2.1, C21.2, C22.2, C25.2, C28.1, C3.1, C30.2, C33.2, C34.2, C4.1, C42.2, C44.2, C45.2, C46.2, C47.2, C48.2, C49.2, C50.2, C51.2, C52.2, C53.1, C56.2, C57.2, C58.1, C60.2, C61.1, C62.2, C63.2, C9.1
- net GND: now also C1.1, C10.1, C11.1, C12.1, C13.2, C14.2, C15.2, C16.2, C17.2, C18.2, C2.1, C20.2, C21.2, C22.2, C24.1, C25.2, C26.1, C27.1, C28.1, C3.1, C30.2, C31.2, C33.2, C34.2, C35.2, C39.1, C4.1, C40.1, C41.1, C42.2, C43.2, C44.2, C45.2, C46.2, C47.2, C48.2, C49.2, C5.2, C50.2, C51.2, C52.2, C53.1, C54.2, C55.2, C56.2, C57.2, C58.1, C6.2, C60.2, C61.1, C62.2, C63.2, C65.1, C66.1, C67.1, C68.1, C69.1, C7.2, C70.1, C71.1, C72.1, C8.2, C9.1; no longer C1.2, C10.2, C11.2, C12.2, C13.1, C14.1, C15.1, C16.1, C17.1, C18.1, C2.2, C20.1, C21.1, C22.1, C24.2, C25.1, C26.2, C27.2, C28.2, C3.2, C30.1, C31.1, C33.1, C34.1, C35.1, C39.2, C4.2, C40.2, C41.2, C42.1, C43.1, C44.1, C45.1, C46.1, C47.1, C48.1, C49.1, C5.1, C50.1, C51.1, C52.1, C53.2, C54.1, C55.1, C56.1, C57.1, C58.2, C6.1, C60.1, C61.2, C62.1, C63.1, C7.1, C8.1, C9.2
- net N$31: now also C24.2; no longer C24.1
- net N$8: now also C20.1; no longer C20.2
- net N$9: now also C18.1; no longer C18.2
- net VREF/VOUT: now also C13.1, C14.1, C15.1, C16.1, C5.1, C6.1, C7.1, C8.1; no longer C13.2, C14.2, C15.2, C16.2, C5.2, C6.2, C7.2, C8.2
- net VUSB: now also C26.2, C27.2, C40.2, C41.2; no longer C26.1, C27.1, C40.1, C41.1
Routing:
- net 3V3: track 573.9 -> 586.3 mm
- net VREF/VOUT: track 187.0 -> 191.3 mm
- net BPIO1: track 58.7 -> 56.1 mm
- net BUFDIR4: track 22.1 -> 20.4 mm
- net BPIO4: track 55.2 -> 56.4 mm
- net BUFDIR1: track 19.5 -> 18.4 mm
- net BUFDIR2: track 25.8 -> 24.9 mm
- net BUFDIR3: track 13.7 -> 13.1 mm
- net BUFDIR0: track 28.8 -> 28.2 mm
- net BUFDIR6: track 29.7 -> 29.2 mm
- net BPIO2: track 43.3 -> 42.7 mm
- net BUFOD7: track 22.6 -> 23.1 mm
- net BUFOD5: track 9.46 -> 9.96 mm
- net BUFOD4: track 20.2 -> 20.7 mm
- net BUFOD3: track 6.19 -> 6.69 mm
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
